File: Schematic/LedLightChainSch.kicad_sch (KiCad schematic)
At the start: 17 parts, among them J1 Led-Chain, J2 Out+, J3 Out-, J4 Batt+, J5 Batt-, J6 SWDIO, J7 TX, J8 Battery, Q1 BC817, SW1 SW_SPDT, U1 CH32V003JxMx

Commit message: Release with target hardware
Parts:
- U1: footprint Package_SO:JEITA_SOIC-8_3.9x4.9mm_P1.27mm -> Package_DIP:DIP-8_W7.62mm
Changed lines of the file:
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@@
 			)
 		)
-		(property "Footprint" "Package_SO:JEITA_SOIC-8_3.9x4.9mm_P1.27mm"
+		(property "Footprint" "Package_DIP:DIP-8_W7.62mm"
 			(at 93.98 48.26 0)
 			(effects

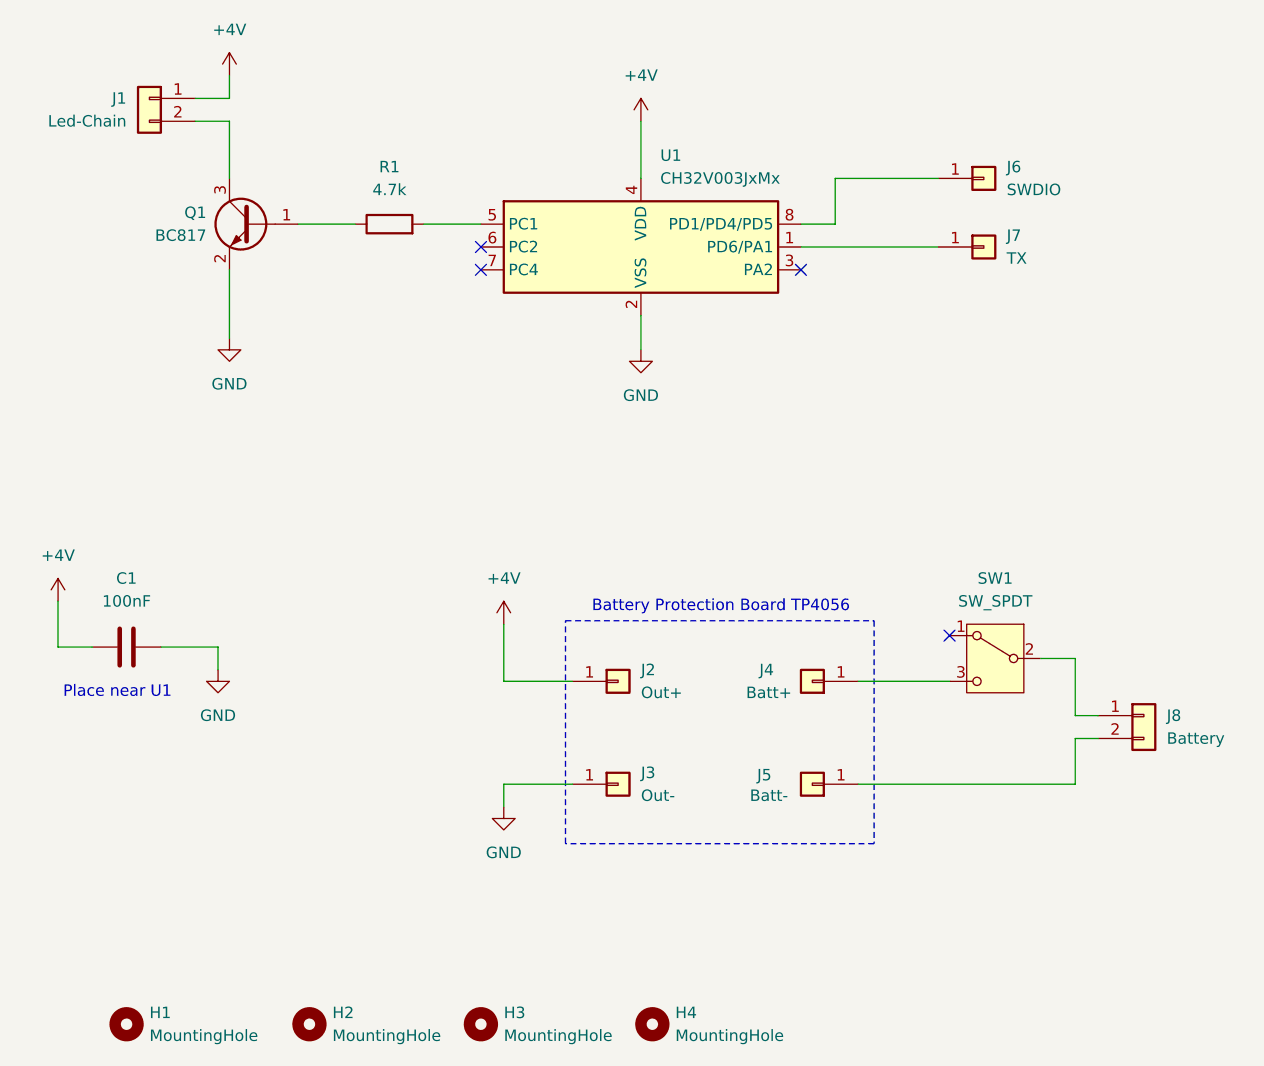
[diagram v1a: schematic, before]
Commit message: PCB Battery-Board connections fixed.
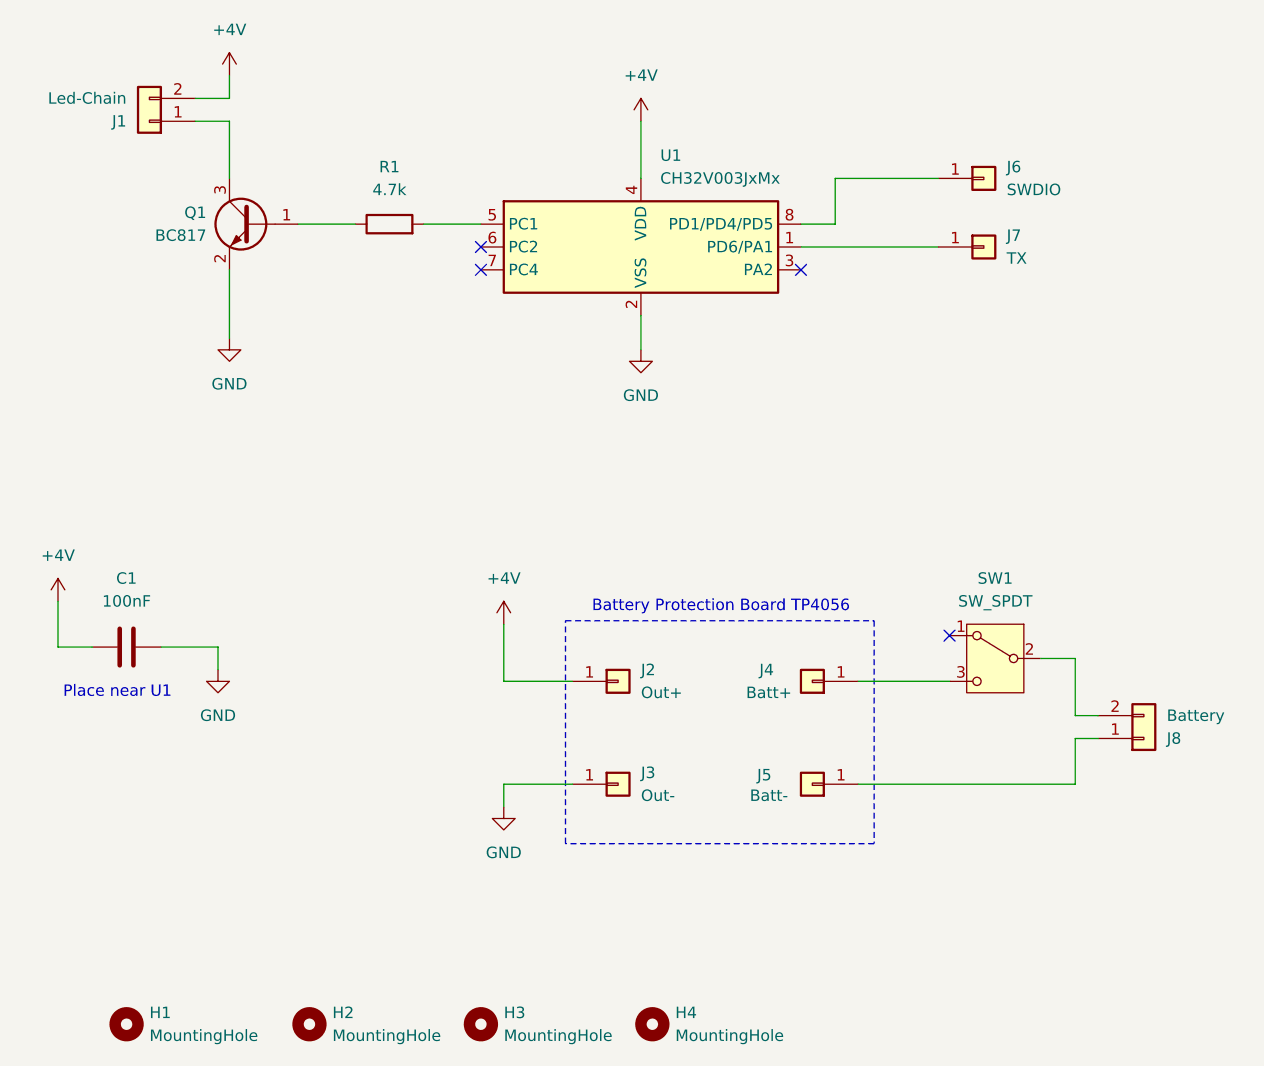
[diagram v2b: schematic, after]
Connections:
- net +4V: now also J1.2 (Pin_2); no longer J1.1 (Pin_1)
- net at J8.1 (Pin_1): now also J5.1 (Pin_1); no longer SW1.2 (B)
- net at J8.2 (Pin_2): now also SW1.2 (B); no longer J5.1 (Pin_1)
- net at Q1.3 (C): now also J1.1 (Pin_1); no longer J1.2 (Pin_2)
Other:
- moved on the sheet: J1
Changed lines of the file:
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@@
 	(symbol
 		(lib_id "Connector_Generic:Conn_01x02")
-		(at 149.86 100.33 0)
-		(unit 1)
-		(exclude_from_sim no)
-		(in_bom yes)
-		(on_board yes)
-		(dnp no)
-		(fields_autoplaced yes)
+		(at 149.86 102.87 0)
+		(mirror x)
+		(unit 1)
+		(exclude_from_sim no)
+		(in_bom yes)
+		(on_board yes)
+		(dnp no)
 		(property "Reference" "J8"
-			(at 152.4 100.3299 0)
+			(at 152.4 102.8701 0)
 			(effects
 				(font
@@
 		)
 		(property "Value" "Battery"
-			(at 152.4 102.8699 0)
+			(at 152.4 100.3301 0)
 			(effects
 				(font
@@
 		)
 		(property "Footprint" "Connector_Molex:Molex_KK-396_A-41792-0002_1x02_P3.96mm_Horizontal"
-			(at 149.86 100.33 0)
+			(at 149.86 102.87 0)
 			(effects
 				(font
@@
 		)
 		(property "Datasheet" "~"
-			(at 149.86 100.33 0)
+			(at 149.86 102.87 0)
 			(effects
 				(font
@@
 		)
 		(property "Description" "Generic connector, single row, 01x02, script generated (kicad-library-utils/schlib/autogen/connector/)"
-			(at 149.86 100.33 0)
+			(at 149.86 102.87 0)
 			(effects
 				(font
@@
 	(symbol
 		(lib_id "Connector_Generic:Conn_01x02")
-		(at 39.37 31.75 0)
-		(mirror y)
+		(at 39.37 34.29 180)
 		(unit 1)
 		(exclude_from_sim no)
@@
 		(dnp no)
 		(property "Reference" "J1"
-			(at 36.83 31.7499 0)
+			(at 36.83 34.2901 0)
 			(effects
 				(font
@@
 		)
 		(property "Value" "Led-Chain"
-			(at 36.83 34.2899 0)
+			(at 36.83 31.7501 0)
 			(effects
 				(font
@@
 		)
 		(property "Footprint" "Connector_PinHeader_2.54mm:PinHeader_1x02_P2.54mm_Vertical"
-			(at 39.37 31.75 0)
+			(at 39.37 34.29 0)
 			(effects
 				(font
@@
 		)
 		(property "Datasheet" "~"
-			(at 39.37 31.75 0)
+			(at 39.37 34.29 0)
 			(effects
 				(font
@@
 		)
 		(property "Description" "Generic connector, single row, 01x02, script generated (kicad-library-utils/schlib/autogen/connector/)"
-			(at 39.37 31.75 0)
-			(effects
-				(font
+			(at 39.37 34.29 0)
+			(effects
+				(font

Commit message: Transistor removed
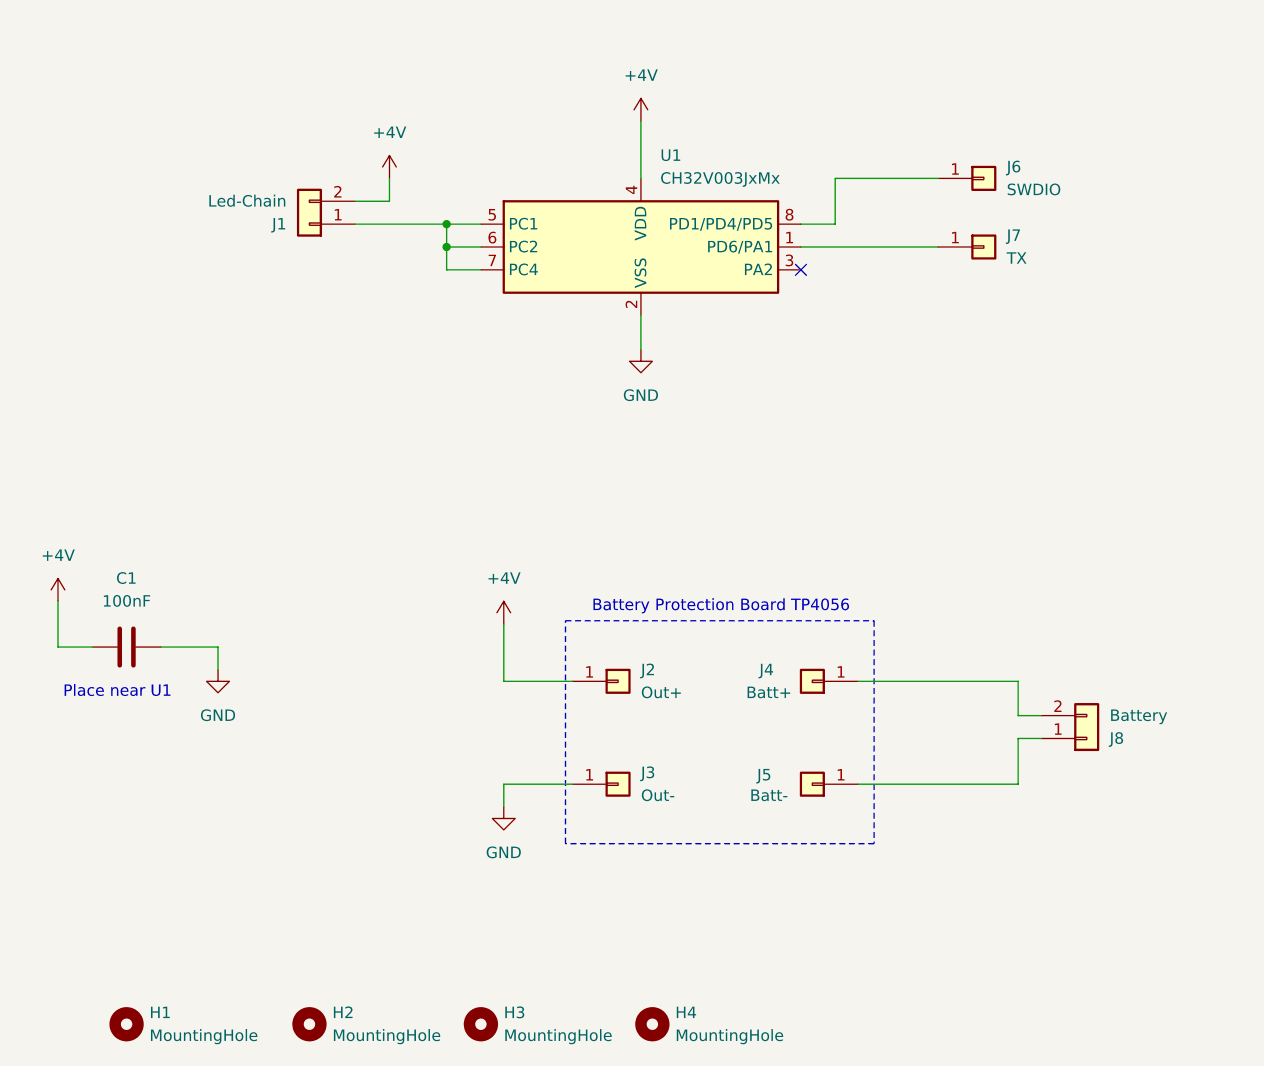
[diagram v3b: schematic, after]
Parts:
- removed Q1: BC817, Package_TO_SOT_SMD:SOT-23, symbol Transistor_BJT:BC817
- removed R1: 4.7k, Resistor_SMD:R_0805_2012Metric_Pad1.20x1.40mm_HandSolder, symbol Device:R
- removed SW1: SW_SPDT, Connector_PinHeader_2.54mm:PinHeader_1x03_P2.54mm_Vertical, symbol Switch:SW_SPDT
- J8: footprint Connector_Molex:Molex_KK-396_A-41792-0002_1x02_P3.96mm_Horizontal -> Connector_PinHeader_2.54mm:PinHeader_1x02_P2.54mm_Vertical
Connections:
- net at J4.1 (Pin_1): now also J8.2 (Pin_2)
- net at U1.5 (PC1): now also J1.1 (Pin_1), U1.6 (PC2), U1.7 (PC4)
- no-connect marks 4 -> 1
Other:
- title: (none) -> LED Light-Chain Timer
- moved on the sheet: J1, J8
